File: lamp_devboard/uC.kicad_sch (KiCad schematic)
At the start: 29 parts, among them J901 Conn_02x05_Odd_Even, J902 Conn_01x03, J903 Conn_01x06, J904 Conn_01x06, J905 Conn_01x06, J906 Conn_01x06, U901 STM32L476RG, Y901 Crystal_GND2, Y902 Crystal_GND2

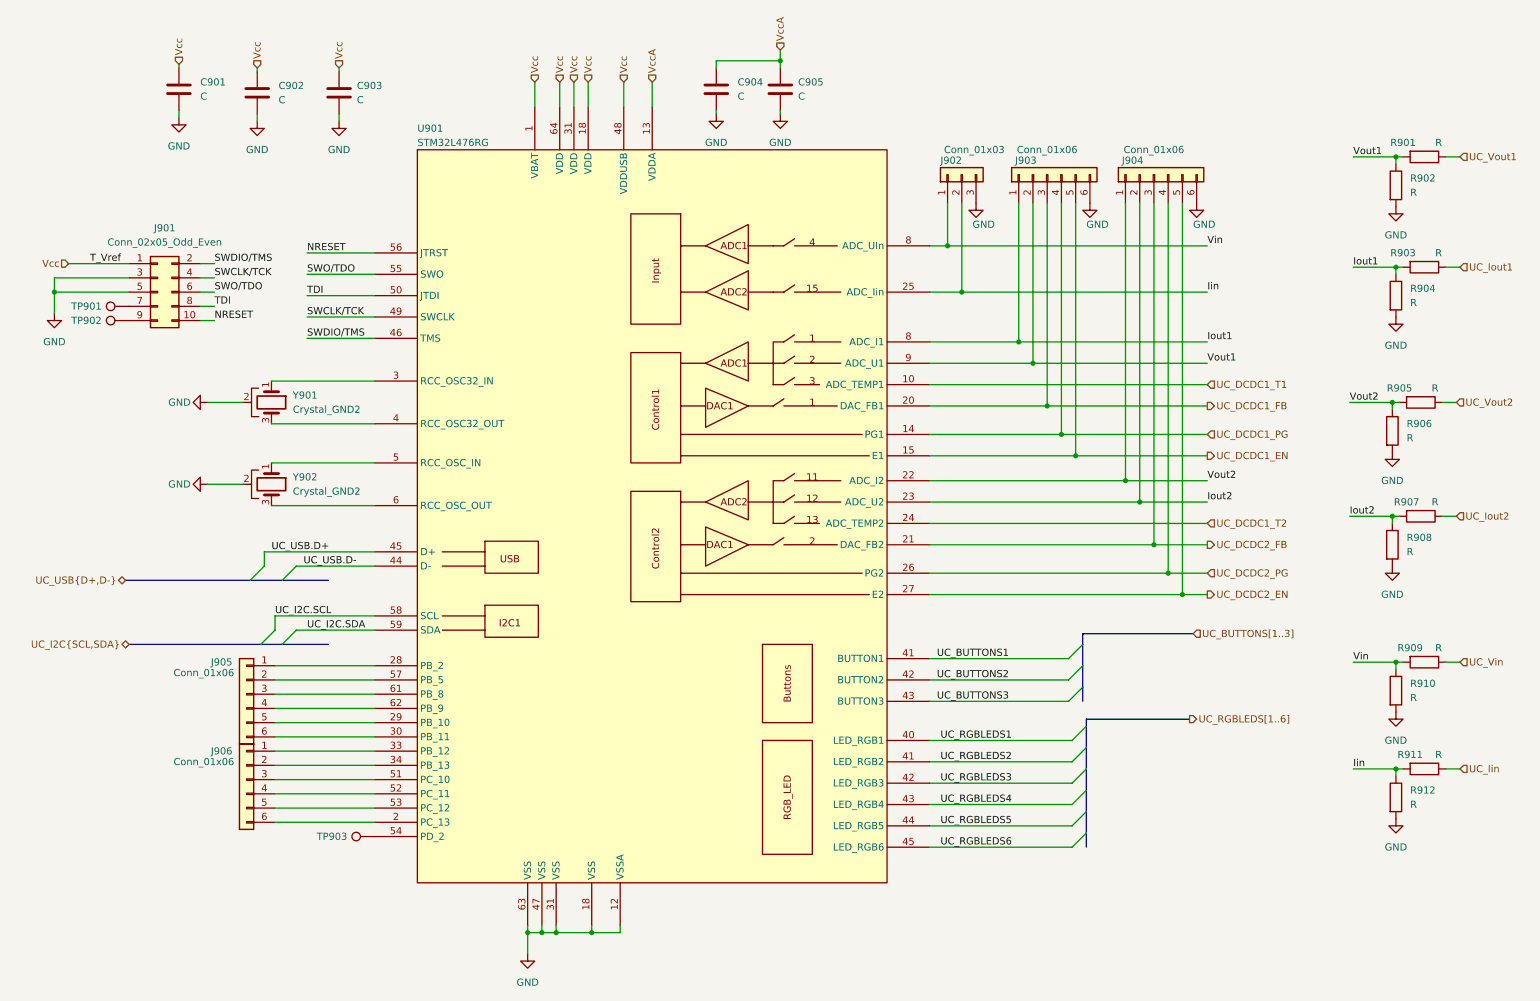
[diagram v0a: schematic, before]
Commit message: schematics, add battery to power module
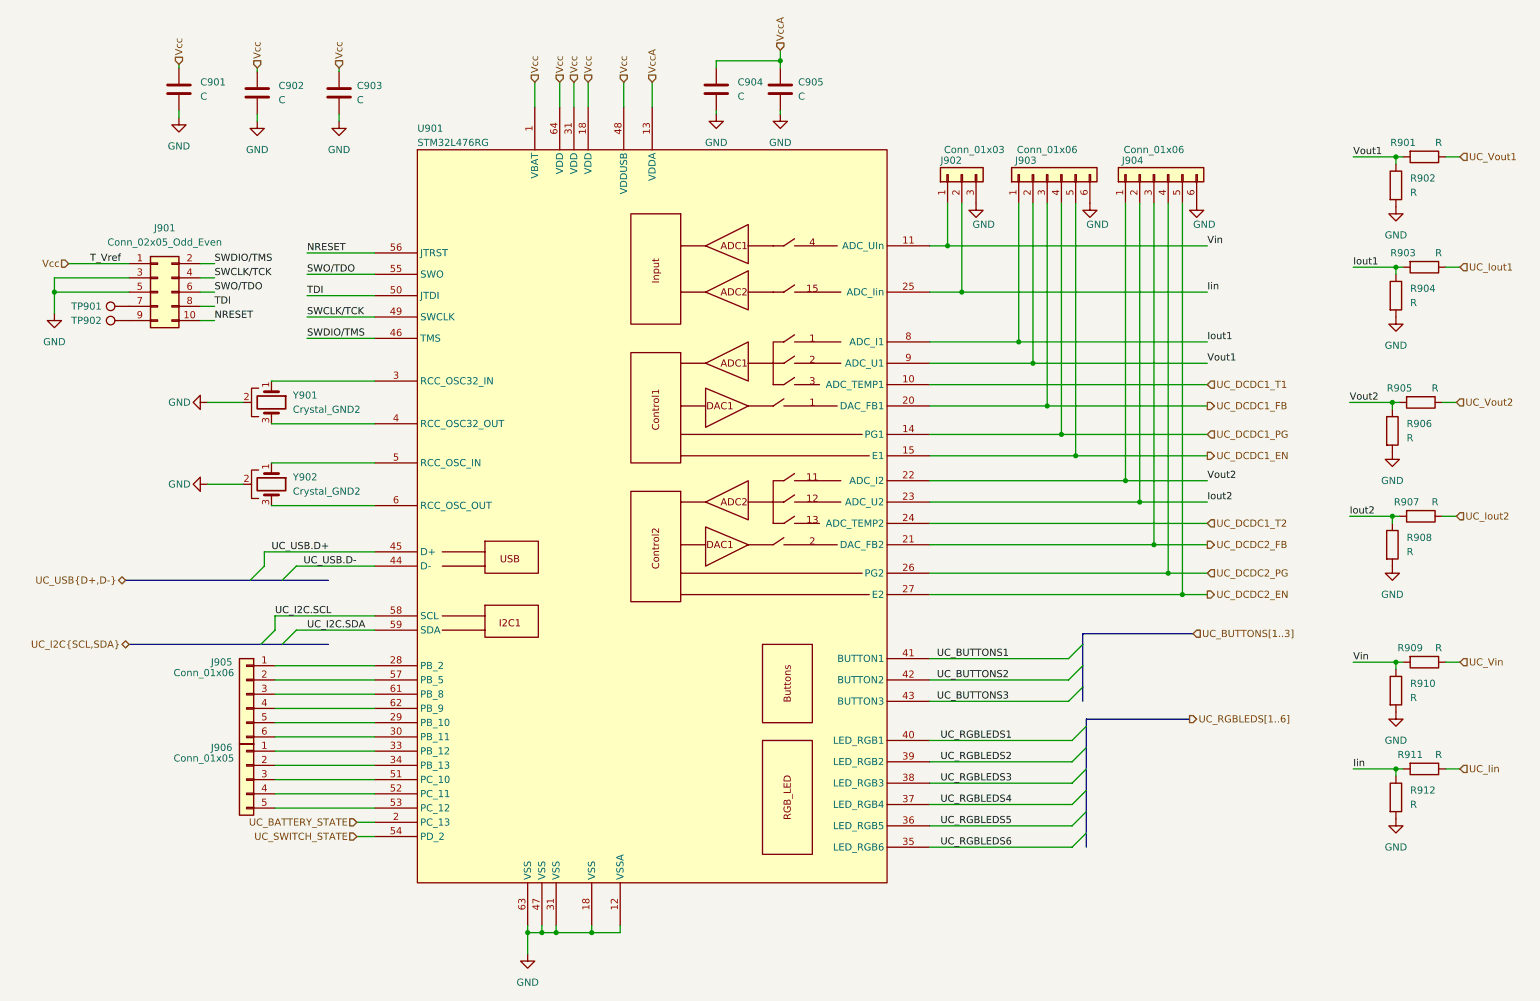
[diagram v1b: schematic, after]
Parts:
- removed J906: Conn_01x06, symbol Connector_Generic:Conn_01x06
- removed TP903: TestPoint, TestPoint:TestPoint_Pad_1.0x1.0mm, symbol Connector:TestPoint
- added J906: Conn_01x05, Connector_PinHeader_2.54mm:PinHeader_1x05_P2.54mm_Vertical, symbol Connector_Generic:Conn_01x05
- J903, J904, J905: footprint (none) -> Connector_PinHeader_2.54mm:PinHeader_1x06_P2.54mm_Vertical
- U901: footprint (none) -> Package_QFP:LQFP-64_10x10mm_P0.5mm
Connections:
- net UC_RGBLEDS2: now also U901.39 (LED_RGB2); no longer U901.41 (LED_RGB2)
- net UC_RGBLEDS3: now also U901.38 (LED_RGB3); no longer U901.42 (LED_RGB3)
- net UC_RGBLEDS4: now also U901.37 (LED_RGB4); no longer U901.43 (LED_RGB4)
- net UC_RGBLEDS5: now also U901.36 (LED_RGB5); no longer U901.44 (LED_RGB5)
- net UC_RGBLEDS6: now also U901.35 (LED_RGB6); no longer U901.45 (LED_RGB6)
- net Vin: now also U901.11 (ADC_UIn); no longer U901.8 (ADC_UIn)
- net UC_BATTERY_STATE: now reaches U901.2 (PC_13)
- net at U901.33 (PB_12): now also J906.1 (Pin_1)
- net at U901.34 (PB_13): now also J906.2 (Pin_2)
- net at U901.51 (PC_10): now also J906.3 (Pin_3)
- net at U901.52 (PC_11): now also J906.4 (Pin_4)
- net at U901.53 (PC_12): now also J906.5 (Pin_5)
- net UC_SWITCH_STATE: now reaches U901.54 (PD_2)

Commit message: place components
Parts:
- Y901, Y902: footprint Crystal:Crystal_SMD_0603-4Pin_6.0x3.5mm_HandSoldering -> Crystal:Crystal_SMD_3225-4Pin_3.2x2.5mm_HandSoldering
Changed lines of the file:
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@@
       (effects (font (size 1.27 1.27)) (justify left))
     )
-    (property "Footprint" "Crystal:Crystal_SMD_0603-4Pin_6.0x3.5mm_HandSoldering" (id 2) (at 57.15 83.185 0)
+    (property "Footprint" "Crystal:Crystal_SMD_3225-4Pin_3.2x2.5mm_HandSoldering" (id 2) (at 57.15 83.185 0)
       (effects (font (size 1.27 1.27)) hide)
     )
@@
       (effects (font (size 1.27 1.27)) (justify left))
     )
-    (property "Footprint" "Crystal:Crystal_SMD_0603-4Pin_6.0x3.5mm_HandSoldering" (id 2) (at 57.15 97.79 0)
+    (property "Footprint" "Crystal:Crystal_SMD_3225-4Pin_3.2x2.5mm_HandSoldering" (id 2) (at 57.15 97.79 0)
       (effects (font (size 1.27 1.27)) hide)
     )

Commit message: some changes
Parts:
- removed C905: C, Capacitor_SMD:C_0603_1608Metric_Pad1.08x0.95mm_HandSolder, symbol Device:C
- removed J902: Conn_01x03, Connector_PinHeader_2.54mm:PinHeader_1x04_P2.54mm_Vertical, symbol Connector_Generic:Conn_01x03
- removed J903, J904: Conn_01x06, Connector_PinHeader_2.54mm:PinHeader_1x06_P2.54mm_Vertical, symbol Connector_Generic:Conn_01x06
- removed J906: Conn_01x05, Connector_PinHeader_2.54mm:PinHeader_1x05_P2.54mm_Vertical, symbol Connector_Generic:Conn_01x05
- removed TP901, TP902: TestPoint, TestPoint:TestPoint_Pad_1.0x1.0mm, symbol Connector:TestPoint
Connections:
- net UC_BUTTONS3: no longer names the net of U901.43 (BUTTON3)
- net UC_RGBLEDS4: no longer names the net of U901.37 (LED_RGB4)
- net UC_RGBLEDS5: no longer names the net of U901.36 (LED_RGB5)
- net UC_RGBLEDS6: no longer names the net of U901.35 (LED_RGB6)
- no-connect marks 0 -> 7

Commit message: some small changes
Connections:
- net GND: now also J905.2 (Pin_2)
- net Vcc: now also J905.1 (Pin_1)
- net at U901.28 (PB_2): no longer J905.1 (Pin_1)
- net at U901.29 (PB_10): no longer J905.5 (Pin_5)
- net at U901.30 (PB_11): no longer J905.6 (Pin_6)
- net at U901.51 (PC_10): now also J905.3 (Pin_3)
- net at U901.52 (PC_11): now also J905.4 (Pin_4)
- net at U901.53 (PC_12): now also J905.5 (Pin_5)
- net at U901.57 (PB_5): now also J905.6 (Pin_6); no longer J905.2 (Pin_2)
- net at U901.61 (PB_8): no longer J905.3 (Pin_3)
- net at U901.62 (PB_9): no longer J905.4 (Pin_4)
- no-connect marks 7 -> 8
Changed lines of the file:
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@@
   (junction (at 257.81 148.59) (diameter 0) (color 0 0 0 0)
   )
-  (no_connect (at 57.785 155.575))
-  (no_connect (at 57.785 153.035))
-  (no_connect (at 57.785 150.495))
-  (no_connect (at 57.785 145.415))
-  (no_connect (at 57.785 147.955))
   (no_connect (at 31.75 68.58))
   (no_connect (at 31.75 66.04))
+  (no_connect (at 57.785 142.875))
+  (no_connect (at 57.785 130.175))
+  (no_connect (at 57.8435 137.795))
+  (no_connect (at 57.785 132.715))
+  (no_connect (at 57.785 140.335))
+  (no_connect (at 57.785 135.255))
   (bus_entry (at 202.565 148.59) (size -2.54 2.54)
     (stroke (width 0) (type default) (color 0 0 0 0))
@@
     (stroke (width 0) (type default) (color 0 0 0 0))
   )
-  (wire (pts (xy 57.785 155.575) (xy 75.565 155.575))
-    (stroke (width 0) (type default) (color 0 0 0 0))
-  )
   (wire (pts (xy 174.625 80.01) (xy 224.155 80.01))
     (stroke (width 0) (type default) (color 0 0 0 0))
@@
     (stroke (width 0) (type default) (color 0 0 0 0))
   )
-  (wire (pts (xy 57.785 150.495) (xy 75.565 150.495))
+  (wire (pts (xy 41.275 150.495) (xy 75.565 150.495))
     (stroke (width 0) (type default) (color 0 0 0 0))
   )
@@
     (stroke (width 0) (type default) (color 0 0 0 0))
   )
+  (wire (pts (xy 41.275 153.035) (xy 75.565 153.035))
+    (stroke (width 0) (type default) (color 0 0 0 0))
+  )
   (wire (pts (xy 44.45 60.96) (xy 46.99 60.96))
     (stroke (width 0) (type default) (color 0 0 0 0))
@@
     (stroke (width 0) (type default) (color 0 0 0 0))
   )
-  (wire (pts (xy 57.785 145.415) (xy 75.565 145.415))
-    (stroke (width 0) (type default) (color 0 0 0 0))
-  )
   (wire (pts (xy 113.665 26.035) (xy 113.665 30.48))
     (stroke (width 0) (type default) (color 0 0 0 0))
@@
     (stroke (width 0) (type default) (color 0 0 0 0))
   )
+  (wire (pts (xy 41.275 145.415) (xy 42.545 145.415))
+    (stroke (width 0) (type default) (color 0 0 0 0))
+  )
   (wire (pts (xy 258.445 83.185) (xy 257.175 83.185))
     (stroke (width 0) (type default) (color 0 0 0 0))
   )
+  (wire (pts (xy 41.275 142.875) (xy 43.18 142.875))
+    (stroke (width 0) (type default) (color 0 0 0 0))
+  )
   (wire (pts (xy 63.5 64.135) (xy 75.565 64.135))
     (stroke (width 0) (type default) (color 0 0 0 0))
@@
     (stroke (width 0) (type default) (color 0 0 0 0))
   )
-  (wire (pts (xy 57.785 153.035) (xy 75.565 153.035))
-    (stroke (width 0) (type default) (color 0 0 0 0))
-  )
   (bus (pts (xy 201.93 130.175) (xy 201.93 126.365))
     (stroke (width 0) (type default) (color 0 0 0 0))
@@
     (stroke (width 0) (type default) (color 0 0 0 0))
   )
-  (wire (pts (xy 57.785 147.955) (xy 75.565 147.955))
+  (wire (pts (xy 41.275 155.575) (xy 75.565 155.575))
+    (stroke (width 0) (type default) (color 0 0 0 0))
+  )
+  (wire (pts (xy 41.275 147.955) (xy 75.565 147.955))
     (stroke (width 0) (type default) (color 0 0 0 0))
   )
@@
   )
   (hierarchical_label "UC_RGBLEDS[1..3]" (shape output) (at 220.98 139.7 0)
+    (effects (font (size 1.27 1.27)) (justify left))
+  )
+  (hierarchical_label "Vcc" (shape input) (at 43.18 142.875 0)
     (effects (font (size 1.27 1.27)) (justify left))
   )
@@
     (pin "31")
     (pin "31")
-    (pin "33")
-    (pin "34")
     (pin "35")
     (pin "36")
@@
     (pin "56")
     (pin "57")
+    (pin "57")
     (pin "58")
     (pin "59")
@@
     (pin "2")
   )
-  (symbol (lib_id "Connector_Generic:Conn_01x06") (at 52.705 135.255 0) (mirror y) (unit 1)
-    (in_bom yes) (on_board yes)
-    (property "Reference" "J905" (id 0) (at 48.26 129.54 0))
-    (property "Value" "Conn_01x06" (id 1) (at 45.085 131.445 0))
-    (property "Footprint" "Connector_PinHeader_2.54mm:PinHeader_1x06_P2.54mm_Vertical" (id 2) (at 52.705 135.255 0)
-      (effects (font (size 1.27 1.27)) hide)
-    )
-    (property "Datasheet" "~" (id 3) (at 52.705 135.255 0)
-      (effects (font (size 1.27 1.27)) hide)
-    )
-    (pin "1")
-    (pin "2")
-    (pin "3")
-    (pin "4")
-    (pin "5")
-    (pin "6")
-  )
   (symbol (lib_id "Connector_Generic:Conn_02x05_Odd_Even") (at 36.83 63.5 0) (unit 1)
     (in_bom yes) (on_board yes) (fields_autoplaced)
@@
     (pin "2")
   )
+  (symbol (lib_id "power:GND") (at 42.545 145.415 90) (unit 1)
+    (in_bom yes) (on_board yes) (fields_autoplaced)
+    (property "Reference" "#PWR0144" (id 0) (at 48.895 145.415 0)
+      (effects (font (size 1.27 1.27)) hide)
+    )
+    (property "Value" "GND" (id 1) (at 46.355 145.4149 90)
+      (effects (font (size 1.27 1.27)) (justify right))
+    )
+    (property "Footprint" "" (id 2) (at 42.545 145.415 0)
+      (effects (font (size 1.27 1.27)) hide)
+    )
+    (property "Datasheet" "" (id 3) (at 42.545 145.415 0)
+      (effects (font (size 1.27 1.27)) hide)
+    )
+    (pin "1")
+  )
+  (symbol (lib_id "Connector_Generic:Conn_01x06") (at 36.195 147.955 0) (mirror y) (unit 1)
+    (in_bom yes) (on_board yes)
+    (property "Reference" "J905" (id 0) (at 31.75 142.24 0))
+    (property "Value" "Conn_01x06" (id 1) (at 28.575 144.145 0))
+    (property "Footprint" "Connector_PinHeader_2.54mm:PinHeader_1x06_P2.54mm_Vertical" (id 2) (at 36.195 147.955 0)
+      (effects (font (size 1.27 1.27)) hide)
+    )
+    (property "Datasheet" "~" (id 3) (at 36.195 147.955 0)
+      (effects (font (size 1.27 1.27)) hide)
+    )
+    (pin "1")
+    (pin "2")
+    (pin "3")
+    (pin "4")
+    (pin "5")
+    (pin "6")
+  )
   (symbol (lib_id "Device:Crystal_GND2") (at 57.15 97.79 270) (unit 1)

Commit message: first version of the pcb board
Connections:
- net at U901.57 (PB_5): now also J905.6 (Pin_6)
